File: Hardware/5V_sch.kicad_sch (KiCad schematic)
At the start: 23 parts, among them IC2 TPS563200DDCR

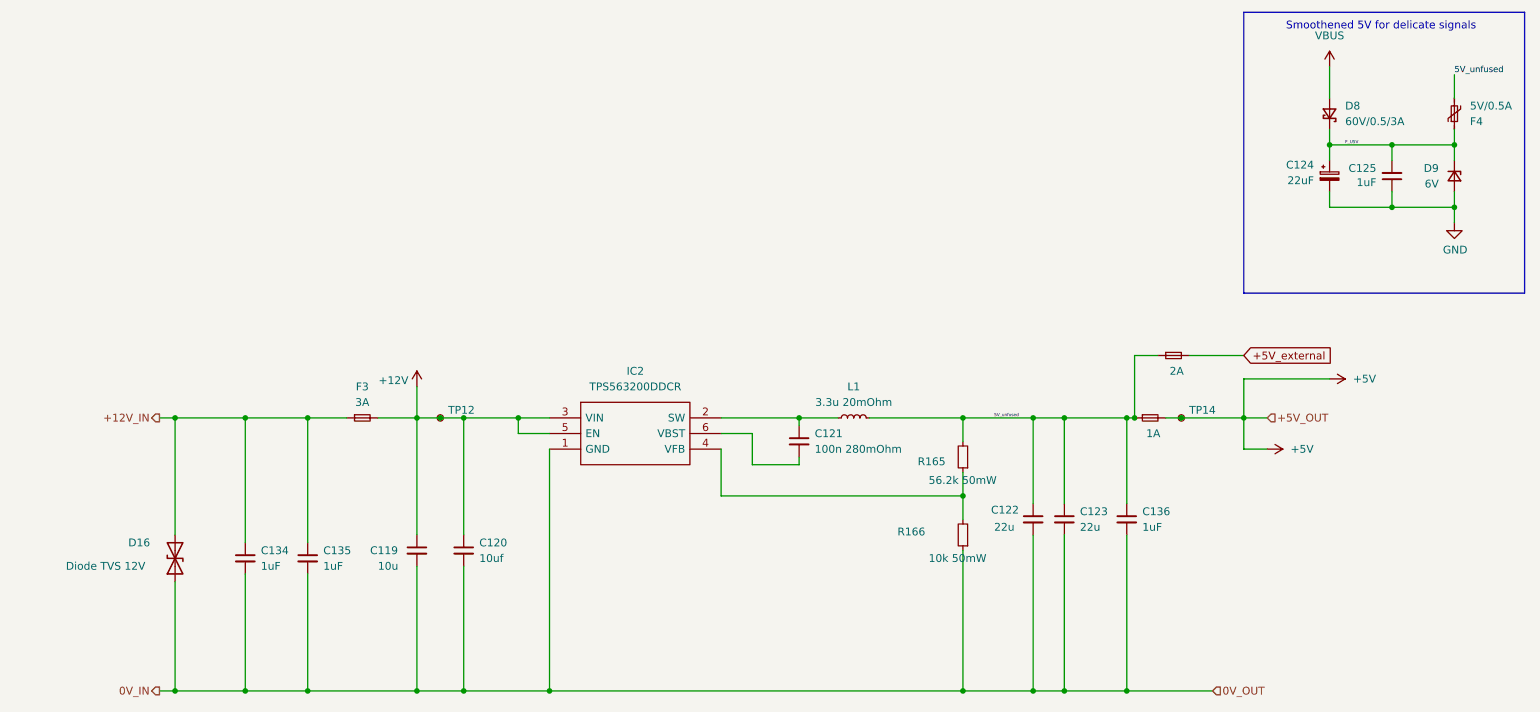
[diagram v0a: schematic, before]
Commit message: Bms plug and play, 2nd iteration with the same pinout
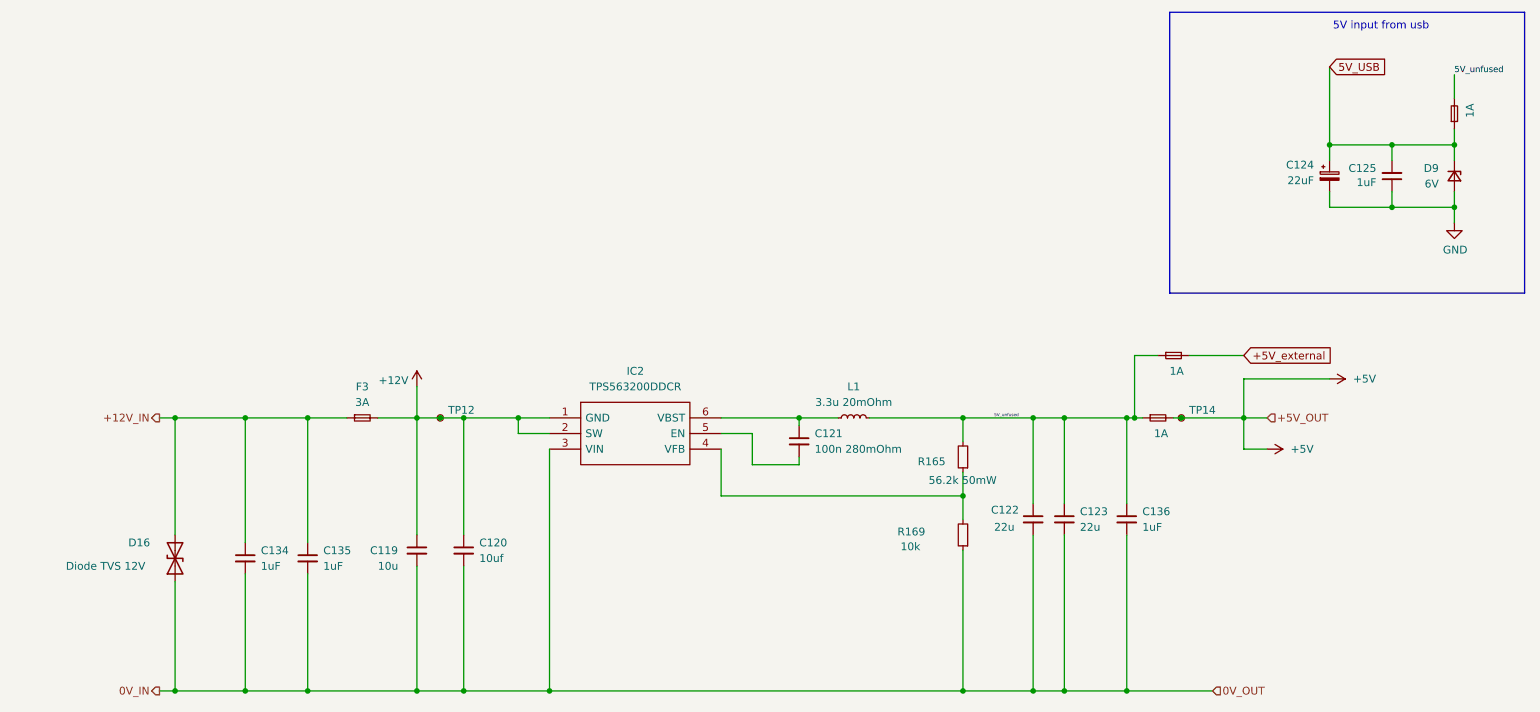
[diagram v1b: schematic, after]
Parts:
- removed D8: 60V/0.5/3A, Diode_SMD:D_SOD-123, symbol Device:D_Schottky_Small
- removed F4: 5V/0.5A, Fuse:Fuse_0805_2012Metric, symbol Device:Polyfuse_Small
- removed R166: 10k 50mW, Resistor_SMD:R_0603_1608Metric_Pad0.98x0.95mm_HandSolder, symbol Device:R_Small
- added F38: 1A, Fuse:Fuse_1206_3216Metric, symbol Device:Fuse_Small
- added R169: 10k, Resistor_SMD:R_0603_1608Metric, symbol Device:R_Small
- F2, F3: footprint Fuse:Fuse_0603_1608Metric_Pad1.05x0.95mm_HandSolder -> Fuse:Fuse_1206_3216Metric
- F6: value 2A -> 1A; footprint Fuse:Fuse_0603_1608Metric_Pad1.05x0.95mm_HandSolder -> Fuse:Fuse_1206_3216Metric
- IC2: footprint footrpint:TPS563200DDCR -> Package_TO_SOT_SMD:SOT-23-6; Description_1 (none) -> 17 V Input, 3A Synchronous Step-Down Regulator in SOT-23 wi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
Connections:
- net +12V: now also IC2.1 (GND), IC2.2 (SW); no longer IC2.3 (VIN), IC2.5 (EN)
- net 0V_IN: now also IC2.3 (VIN), R169.1; no longer IC2.1 (GND)
- net 5V_unfused: now also F38.2
- net at IC2.4 (VFB), R165.1: now also R169.2
- net at C121.1, L1.1: now also IC2.6 (VBST); no longer IC2.2 (SW)
- net at C121.2: now also IC2.5 (EN); no longer IC2.6 (VBST)
- net F_U5V renamed 5V_USB
- net 5V_USB: now also F38.1
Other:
- note added: "5V input from usb"
- note removed: "Smoothened 5V for delicate signals"

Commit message: nearly done
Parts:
- removed F6: 1A, Fuse:Fuse_1206_3216Metric, symbol Device:Fuse_Small
- removed TP12, TP14: TestPoint_Small, TestPoint:TestPoint_Pad_D1.0mm, symbol Connector:TestPoint_Small

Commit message: New connectors jst_xh for low voltage side of bms
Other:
- title: (none) -> Battery Management System for a high power gokart battery
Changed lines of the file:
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@@
 	(generator_version "10.0")
 	(paper "A4")
+	(title_block
+		(title "Battery Management System for a high power gokart battery")
+	)
 	(rectangle
 		(start 225.425 16.51)

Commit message: No drc errors
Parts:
- removed C119: 10u, Capacitor_SMD:C_0805_2012Metric_Pad1.18x1.45mm_HandSolder, symbol Device:C_Small
- removed C120: 10uf, Capacitor_SMD:C_0805_2012Metric_Pad1.18x1.45mm_HandSolder, symbol Device:C_Small
- removed C122, C123: 22u, Capacitor_SMD:C_0603_1608Metric_Pad1.08x0.95mm_HandSolder, symbol Device:C_Small
- removed D16: Diode TVS 12V, Diode_SMD:D_SOD-323F, symbol Device:D_TVS
- added C154, C155, C157: 22u, Capacitor_SMD:C_0805_2012Metric, symbol Device:C_Small
- added C156: 1uF, Resistor_SMD:R_0603_1608Metric, symbol Device:C_Small
- added D44: 13.3V tvs, Package_TO_SOT_SMD:SOT-23, symbol Device:D_TVS_Dual_AAC
- added R170: 10k, Resistor_SMD:R_0603_1608Metric, symbol Device:R_Small
- C121: footprint Capacitor_SMD:C_0805_2012Metric_Pad1.18x1.45mm_HandSolder -> Capacitor_SMD:C_0603_1608Metric
- C134, C135: footprint Capacitor_SMD:C_0603_1608Metric_Pad1.08x0.95mm_HandSolder -> Resistor_SMD:R_0603_1608Metric
- C136: value 1uF -> 22u; footprint Capacitor_SMD:C_0603_1608Metric_Pad1.08x0.95mm_HandSolder -> Capacitor_SMD:C_0805_2012Metric; Field5 (none) -> 22u 3.71mOhm
- L1: value 3.3u 20mOhm -> 4.7u; footprint footrpint:CLF7045__ -> Inductor_SMD:L_Murata_LQH55DN_5.7x5.0mm
- R165: value 56.2k 50mW -> 54.9k; footprint Resistor_SMD:R_0603_1608Metric_Pad0.98x0.95mm_HandSolder -> Resistor_SMD:R_0603_1608Metric
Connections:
- net +12V: now also C134.1, C135.1, IC2.3 (VIN), C155.1, C157.1, D44.1 (A1), D44.2 (A2), R170.2; no longer IC2.1 (GND), IC2.2 (SW)
- net +12V_IN: no longer C134.1, C135.1
- net 0V_IN: now also IC2.1 (GND), C154.2, C155.2, C156.2, C157.2, D44.3 (common); no longer IC2.3 (VIN)
- net 5V_unfused: now also C154.1, C156.1
- net at IC2.5 (EN): now also R170.1; no longer C121.2
- net at C121.1, IC2.6 (VBST): no longer L1.1
- new net: C121.2, IC2.2 (SW), L1.1
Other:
- moved on the sheet: C121, C134, C135, F3, IC2

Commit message: Wysłane do JLC
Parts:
- removed C124: 22uF, Capacitor_SMD:CP_Elec_4x5.8, symbol Device:C_Polarized_Small
- added C126: 22u, Capacitor_SMD:C_1206_3216Metric, symbol Device:C_Small
- L1: footprint Inductor_SMD:L_Murata_LQH55DN_5.7x5.0mm -> Inductor_SMD:L_TDK_VLS6045EX_VLS6045AF
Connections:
- net 5V_USB: now also C126.2
- net GND: now also C126.1
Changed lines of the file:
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@@
+	)
+	(symbol
+		(lib_id "Device:C_Small")
+		(at 251.46 43.18 180)
+		(unit 1)
+		(body_style 1)
+		(exclude_from_sim no)
+		(in_bom yes)
+		(on_board yes)
+		(in_pos_files yes)
+		(dnp no)
+		(property "Reference" "C126"
+			(at 248.92 41.91 0)
+			(show_name no)
+			(do_not_autoplace no)
+			(effects
+				(font
+					(size 1.27 1.27)
+				)
+				(justify left)
+			)
+		)
+		(property "Value" "22u"
+			(at 248.92 44.2214 0)
+			(show_name no)
+			(do_not_autoplace no)
+			(effects
+				(font
+					(size 1.27 1.27)
+				)
+				(justify left)
+			)
+		)
+		(property "Footprint" "Capacitor_SMD:C_1206_3216Metric"
+			(at 251.46 43.18 0)
+			(hide yes)
+			(show_name no)
+			(do_not_autoplace no)
+			(effects
+				(font
+					(size 1.27 1.27)
+				)
+			)
+		)
+		(property "Datasheet" ""
+			(at 251.46 43.18 0)
+			(hide yes)
+			(show_name no)
+			(do_not_autoplace no)
+			(effects
+				(font
+					(size 1.27 1.27)
+				)
+			)
+		)
+		(property "Description" "Unpolarized capacitor, small symbol"
+			(at 251.46 43.18 0)
+			(hide yes)
+			(show_name no)
+			(do_not_autoplace no)
+			(effects
+				(font
+					(size 1.27 1.27)
+				)
+			)
+		)
+		(property "Manufacturer_Name" "--"
+			(at 251.46 43.18 0)
+			(hide yes)
+			(show_name no)
+			(do_not_autoplace no)
+			(effects
+				(font
+					(size 1.27 1.27)
+				)
+			)
+		)
+		(property "Manufacturer_Part_Number" "C0603C104J3RACTU"
+			(at 251.46 43.18 0)
+			(hide yes)
+			(show_name no)
+			(do_not_autoplace no)
+			(effects
+				(font
+					(size 1.27 1.27)
+				)
+			)
+		)
+		(property "In Order" ""
+			(at 251.46 43.18 0)
+			(hide yes)
+			(show_name no)
+			(do_not_autoplace no)
+			(effects
+				(font
+					(size 1.27 1.27)
+				)
+			)
+		)
+		(property "Mouser Part Number" "80-C0603C104J3R"
+			(at 251.46 43.18 0)
+			(hide yes)
+			(show_name no)
+			(do_not_autoplace no)
+			(effects
+				(font
+					(size 1.27 1.27)
+				)
+			)
+		)
+		(property "Mouser Price/Stock" "https://www.mouser.pl/ProductDetail/KEMET/C0603C104J3RACTU?qs=EHsFn6hSx4W0Oy0I8JUofQ%3D%3D"
+			(at 251.46 43.18 0)
+			(hide yes)
+			(show_name no)
+			(do_not_autoplace no)
+			(effects
+				(font
+					(size 1.27 1.27)
+				)
+			)
+		)
+		(property "Arrow Part Number" ""
+			(at 251.46 43.18 0)
+			(hide yes)
+			(show_name no)
+			(do_not_autoplace no)
+			(effects
+				(font
+					(size 1.27 1.27)
+				)
+			)
+		)
+		(property "Arrow Price/Stock" ""
+			(at 251.46 43.18 0)
+			(hide yes)
+			(show_name no)
+			(do_not_autoplace no)
+			(effects
+				(font
+					(size 1.27 1.27)
+				)
+			)
+		)
+		(pin "1"
+		)
+		(pin "2"
+		)
+		(instances
+			(project "BMS"
+				(path "/26289bb6-56bc-4ca1-b1a2-18d58d1afdf5/b306fb08-ef5e-4bf5-8efa-c4e5200f566a/3120d456-738f-4dcb-b831-006287d4ee74"
+					(reference "C126")
+					(unit 1)
+				)
+			)
+		)
 	)
 	(symbol
@@
 				(path "/26289bb6-56bc-4ca1-b1a2-18d58d1afdf5/b306fb08-ef5e-4bf5-8efa-c4e5200f566a/3120d456-738f-4dcb-b831-006287d4ee74"
 					(reference "R165")
-					(unit 1)
-				)
-			)
-		)
-	)
-	(symbol
-		(lib_id "Device:C_Polarized_Small")
-		(at 251.46 43.18 0)
-		(unit 1)
-		(body_style 1)
-		(exclude_from_sim no)
-		(in_bom yes)
-		(on_board yes)
-		(in_pos_files yes)
-		(dnp no)
-		(property "Reference" "C124"
-			(at 248.92 41.3638 0)
-			(show_name no)
-			(do_not_autoplace no)
-			(effects
-				(font
-					(size 1.27 1.27)
-				)
-				(justify right)
-			)
-		)
-		(property "Value" "22uF"
-			(at 248.92 43.9038 0)
-			(show_name no)
-			(do_not_autoplace no)
-			(effects
-				(font
-					(size 1.27 1.27)
-				)
-				(justify right)
-			)
-		)
-		(property "Footprint" "Capacitor_SMD:CP_Elec_4x5.8"
-			(at 251.46 43.18 0)
-			(hide yes)
-			(show_name no)
-			(do_not_autoplace no)
-			(effects
-				(font
-					(size 1.27 1.27)
-				)
-			)
-		)
-		(property "Datasheet" ""
-			(at 251.46 43.18 0)
-			(hide yes)
-			(show_name no)
-			(do_not_autoplace no)
-			(effects
-				(font
-					(size 1.27 1.27)
-				)
-			)
-		)
-		(property "Description" "Polarized capacitor, small symbol"
-			(at 251.46 43.18 0)
-			(hide yes)
-			(show_name no)
-			(do_not_autoplace no)
-			(effects
-				(font
-					(size 1.27 1.27)
-				)
-			)
-		)
-		(property "Mouser Price/Stock" "https://www.mouser.pl/ProductDetail/Samsung-Electro-Mechanics/CL21A107MQYNNWE?qs=81r%252BiQLm7BSNi6fWCnDBNQ%3D%3D"
-			(at 251.46 43.18 0)
-			(hide yes)
-			(show_name no)
-			(do_not_autoplace no)
-			(effects
-				(font
-					(size 1.27 1.27)
-				)
-			)
-		)
-		(property "Mouser Part Number" "647-UCM1V220MCL1GS"
-			(at 251.46 43.18 0)
-			(hide yes)
-			(show_name no)
-			(do_not_autoplace no)
-			(effects
-				(font
-					(size 1.27 1.27)
-				)
-			)
-		)
-		(pin "1"
-		)
-		(pin "2"
-		)
-		(instances
-			(project "BMS"
-				(path "/26289bb6-56bc-4ca1-b1a2-18d58d1afdf5/b306fb08-ef5e-4bf5-8efa-c4e5200f566a/3120d456-738f-4dcb-b831-006287d4ee74"
-					(reference "C124")
 					(unit 1)
 				)
@@
 			)
 		)
-		(property "Footprint" "Inductor_SMD:L_Murata_LQH55DN_5.7x5.0mm"
+		(property "Footprint" "Inductor_SMD:L_TDK_VLS6045EX_VLS6045AF"
 			(at 173.99 82.55 0)
 			(hide yes)
@@
 			)
 		)
-		(property "Datasheet" "https://www.mouser.pl/ProductDetail/TDK/CLF7045NIT-3R3N-D?qs=P8zzrVhehaveWwbrqo7%252Bdg%3D%3D"
+		(property "Datasheet" "https://www.mouser.pl/pl/ProductDetail/Pulse-Electronics/BWVS006060454R7ML1?qs=DRkmTr78QARVNxIXd%2Fq4pA%3D%3D"
 			(at 173.99 82.55 0)
 			(hide yes)
@@
 			)
 		)
-		(property "Description" "LQH55DN4R7M03L"
+		(property "Description" "BWVS006060454R7ML1"
 			(at 173.99 82.55 0)
 			(hide yes)
